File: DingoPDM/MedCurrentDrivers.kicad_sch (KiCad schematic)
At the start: 2 parts, among them U21 LM324

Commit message: Added documentation, finished and cleaned design
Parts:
- R53: LCSC (none) -> C727987
- U21: Digi-Key_PN (none) -> 497-7330-1-ND; LCSC (none) -> C7944
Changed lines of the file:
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@@
   (title_block
     (title "Dingo_PDM")
-    (date "2023-04-01")
-    (rev "v5")
+    (date "2023-07-28")
+    (rev "v6")
     (comment 3 "github.com/corygrant")
     (comment 4 "Cory Grant")
@@
       (effects (font (size 1.27 1.27)) hide)
     )
-    (property "LCSC" "" (at 121.285 47.625 0)
+    (property "LCSC" "C727987" (at 121.285 47.625 0)
       (effects (font (size 1.27 1.27)) hide)
     )
@@
       (effects (font (size 1.27 1.27)) hide)
     )
+    (property "Digi-Key_PN" "497-7330-1-ND" (at 108.585 47.625 0)
+      (effects (font (size 1.27 1.27)) hide)
+    )
+    (property "LCSC" "C7944" (at 108.585 47.625 0)
+      (effects (font (size 1.27 1.27)) hide)
+    )

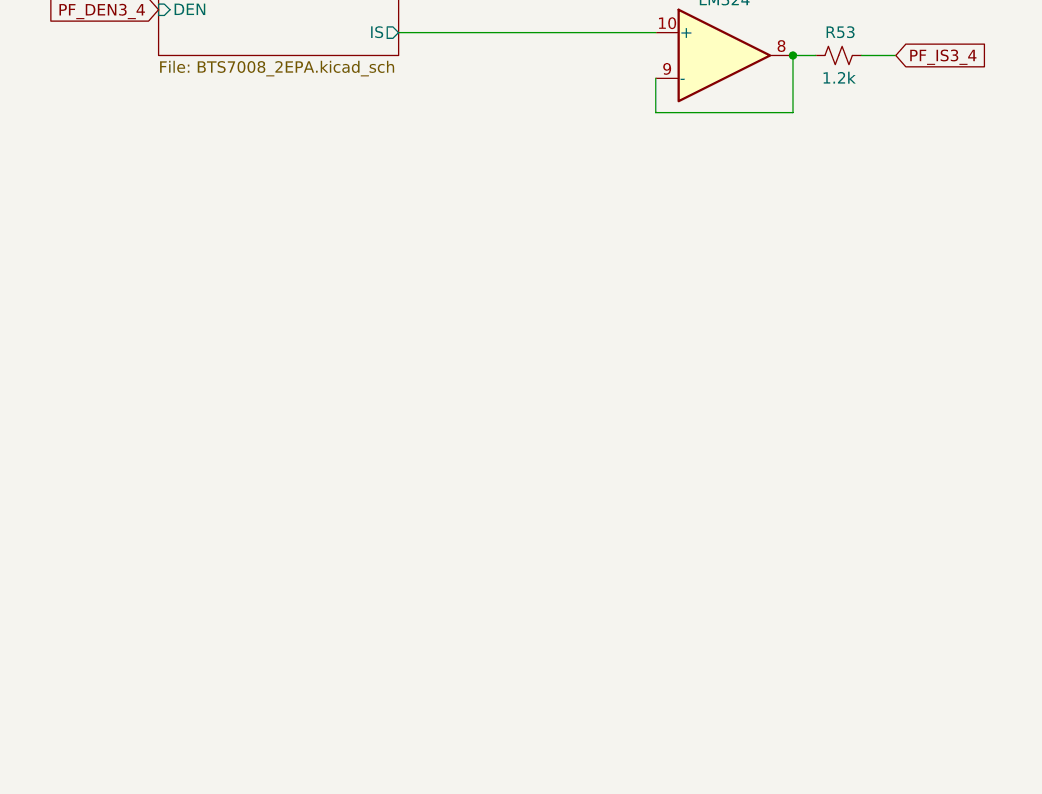
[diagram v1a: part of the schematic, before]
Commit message: Changed to STM32F446RE
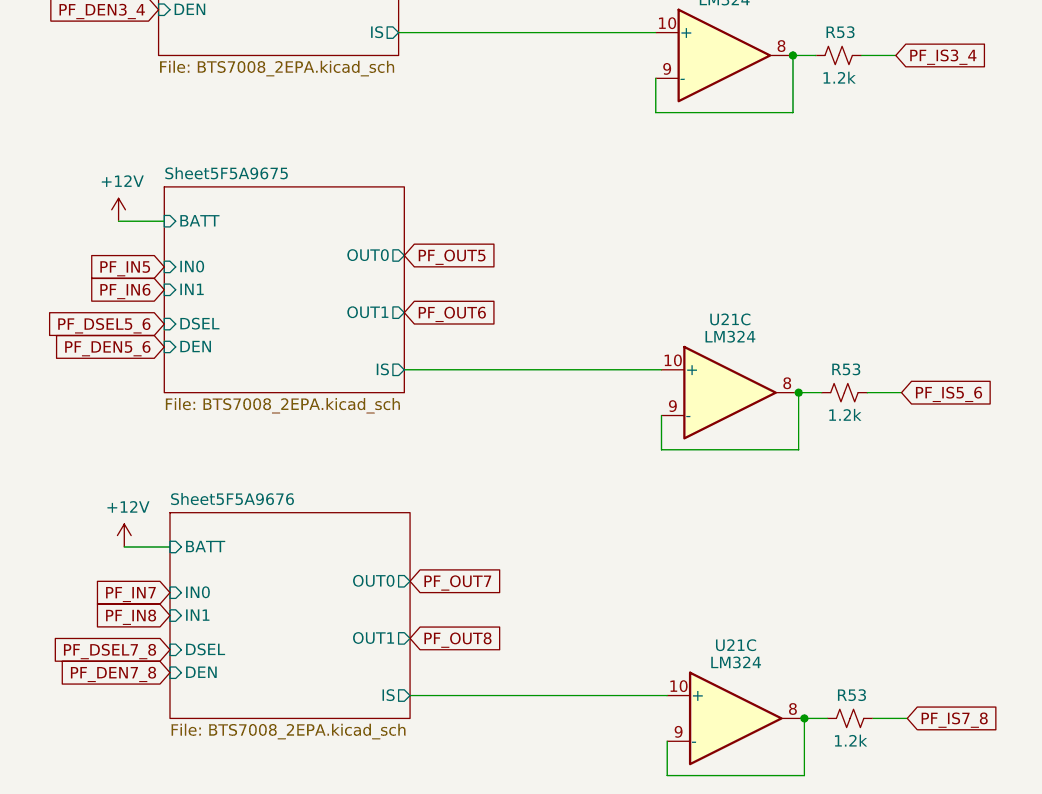
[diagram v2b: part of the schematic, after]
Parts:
- added R53 (x2): 1.2k, Resistor_SMD:R_0805_2012Metric, symbol Device:R_Small_US
- added U21 (x2): LM324, Package_SO:TSSOP-14_4.4x5mm_P0.65mm, symbol Amplifier_Operational:LM324
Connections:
- new net: R53.1, U21.8, U21.9 (-) (x2)
- new net PF_IS5_6: R53.2
- new net PF_IS7_8: R53.2
- new net Sheet5F5A9675/IS: U21.10 (+)
- new net Sheet5F5A9676/IS: U21.10 (+)
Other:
- added sheet Sheet5F5A9675 (BTS7008_2EPA.kicad_sch)
- added sheet Sheet5F5A9676 (BTS7008_2EPA.kicad_sch)

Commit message: Routed V7
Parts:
- removed R53 (x3): 1.2k, Resistor_SMD:R_0805_2012Metric, symbol Device:R_Small_US
- added C41: 100nF, Capacitor_SMD:C_0805_2012Metric, symbol Device:C_Small
- added R8 (x3): 120R, Resistor_SMD:R_0805_2012Metric, symbol Device:R_Small_US
- added U7: LM324, Package_SO:TSSOP-14_4.4x5mm_P0.65mm, symbol Amplifier_Operational:LM324
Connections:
- net PF_IS3_4: now also R8.1
- net PF_IS5_6: now also R8.1
- net PF_IS7_8: now also R8.1
- net at U21.8, U21.9 (-): now also R8.2 (x3)
- new net +3V3: C41.2, U7.4 (V+)
- new net GND: C41.1, U7.11 (V-)

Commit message: Update JLC part numbers for in stock ones
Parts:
- U21, U7: LCSC C7944 -> C7942
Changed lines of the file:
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@@
       (effects (font (size 1.27 1.27)) hide)
     )
-    (property "LCSC" "C7944" (at 248.285 34.925 0)
+    (property "LCSC" "C7942" (at 248.285 34.925 0)
       (effects (font (size 1.27 1.27)) hide)
     )
@@
       (effects (font (size 1.27 1.27)) hide)
     )
-    (property "LCSC" "C7944" (at 109.855 121.285 0)
+    (property "LCSC" "C7942" (at 109.855 121.285 0)
       (effects (font (size 1.27 1.27)) hide)
     )
@@
       (effects (font (size 1.27 1.27)) hide)
     )
-    (property "LCSC" "C7944" (at 109.22 85.09 0)
+    (property "LCSC" "C7942" (at 109.22 85.09 0)
       (effects (font (size 1.27 1.27)) hide)
     )
@@
       (effects (font (size 1.27 1.27)) hide)
     )
-    (property "LCSC" "C7944" (at 108.585 47.625 0)
-      (effects (font (size 1.27 1.27)) hide)
-    )
+    (property "LCSC" "C7942" (at 108.585 47.625 0)
+      (effects (font (size 1.27 1.27)) hide)
+    )
